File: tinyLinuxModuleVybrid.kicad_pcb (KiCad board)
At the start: 4 copper layers, 85 x 56 mm, 164 parts, among them IC1 LAN8720, IC2 USB2514B, IC3 MAX3221, IC4 TPS2033, IC5 WE-TVS-82400274, IC6 WE-TVS-82400274, IC7 TLV62065, M1 SCREW, M2 SCREW, M3 SCREW, M4 SCREW, M5 SCREW, M6 SCREW, M7 SCREW, M8 SCREW, Q1 2N7002BKT, Q2 2N7002BKT, Q3 2N7002BKT, U1 LT3958, X1 CONN_02x50, X10 MagJack100, X11 MICROSD, X12 CONN_01x03, X2 CONN_02x50, X3 USB4DUAL, X4 CONN_02x25, X5 ARM_JTAG_10, X6 USB4DUAL, X7 CONN_02x20, X8 CONN_02x14, X9 USB5, Y1 24M,18p

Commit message: LILY Antenne hinzugefügt
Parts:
- added REF**: NANO_SIM_693043020611, Connector:NANO_SIM_693043020611, F.Cu at (22.0, -51.4)
- moved REF** 108.0 mm to (25.3, -26.1), turned to 90 degrees
- moved X? 96.1 mm to (39.1, -8.16)
- moved U1 46.9 mm to (75.1, -27.8)
- moved L1 45.1 mm to (70.8, -30.2)
- moved REF** 22.3 mm to (7.78, -26.8)
- moved REF** 20.2 mm to (4.51, -15.4), turned to 90 degrees
- moved REF** 13.2 mm to (5.04, -39.9)
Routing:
- net GND: track 164.5 -> 406.0 mm, vias 99 -> 111
- net (no net): track 1257.1 -> 1033.4 mm, vias 56 -> 33
- net +3V3: track 120.9 -> 273.9 mm, vias 30 -> 39
- net /PTC6: track 0.00 -> 55.8 mm, vias 0 -> 3
- net +5V: track 117.3 -> 69.6 mm, vias 7 -> 1
- net /PTE21: track 33.8 -> 1.46 mm, vias 3 -> 0
- net /PTC4: track 76.4 -> 45.7 mm, vias 3 -> 1
- net /PTE15: track 30.6 -> 2.03 mm, vias 3 -> 0
- net /PTE17: track 26.6 -> 1.46 mm, vias 3 -> 1
- net /PTC1: track 73.1 -> 56.7 mm, vias 3 -> 4
- net /PTE9: track 35.4 -> 20.4 mm, vias 3 -> 1
- net /PTE19: track 22.5 -> 7.50 mm, vias 3 -> 2
- net /PTE13: track 3.10 -> 17.6 mm, vias 0 -> 1
- net /PTE10: track 0.00 -> 13.5 mm, vias 0 -> 1
- net /Communication/RMII_TXEN: track 15.6 -> 2.56 mm, vias 2 -> 0
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
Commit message: added some footprints
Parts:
- removed C1, C12, C14, C15, C33 (x3), C35, C37, C38, C39, C40 (x3): 22u,10V, Passives:C1206N
- removed C10, C11, C2, C3, C32 (x3), C4, C8: 100n, Passives:C0402N
- removed C16, C17, C18, C19, C20, C21, C22, C41: 1u,10V,X5R, Passives:C0402N
- removed C23, C24, C25, C26: 10p, Passives:C0402N
- removed C27, C28, C29, C30, C31: 100n,16V, Passives:C0402N
- removed C34: 220u,16V, Passives:CPOL_THT_D6.3_G2.5
- removed C36: 22p,25V, Passives:C0402N
- removed C6, C7: 18p, Passives:C0402N
- removed FID1, FID2, FID3 (x3), FID4: FIDUCIAL, Mechanical:FIDUCIAL_1mm
- removed IC1: LAN8720, Communication:LAN8720_QFN33
- removed IC2: USB2514B, USB_IC:USB251xB_QFN36
- removed IC3: MAX3221, Communication:MAX3221_TSSOP
- removed IC4: TPS2033, USB_IC:TPS203xD
- removed IC5, IC6: WE-TVS-82400274, USB_IC:WE-TVS-82400274_SC70
- removed IC7: TLV62065, Switcher_IC:TLV62065_WSON
- removed L1: 600R@100M, Passives:B0402N
- removed L1: DRQ125, myfootprint:DRQ125
- removed L2: 1uH,2A, Passives:L1008N
- removed LED1 (x3): G, Passives:LED0603N
- removed LED2 (x3): Y, Passives:LED0603N
- removed LED3 (x3): B, Passives:LED0603N
- removed M1, M2, M3, M4: SCREW, Mechanical:SCREW_M1.5
- removed M5, M6, M7, M8: SCREW, Mechanical:SCREW_M2.5
- removed PTC1: 2A, Passives:PTC1210N
- removed Q1 (x3), Q2 (x3), Q3 (x3): 2N7002BKT, Transistor:SOT416_GSD
- removed R10 (x3), R11 (x3), R13, R16, R35 (x3), R36 (x3), R6, R7, R8 (x3), R9 (x3): 10k, Passives:R0402N
- removed R12, R14: 470, Passives:R0402N
- removed R15, R25 (x3), R26 (x3), R27 (x3), R31 (x3), R32 (x3), R33 (x3): 1k, Passives:R0402N
- removed R17, R5: 12k, Passives:R0402N
- removed R18, R19, R20, R21: 49.9R, Passives:R0402N
- removed R22: 22R, Passives:R0402N
- removed R29: 390k, Passives:R0402N
- removed R30: 86.6k, Passives:R0402N
- removed R37: 22, Passives:R0402N
- removed REF**: MPU-9250, Sensors:MPU-9250
- removed REF**: LILY-W1, Communication:UBLOX-LILY-W1
- removed REF**: NEO-M8P, Communication:UBLOX_NEO-M8P
- removed REF**: Toby L210, Communication:UBLOX_TOBY_L210
- removed REF**: NANO_SIM_693043020611, Connector:NANO_SIM_693043020611
- removed U1: LT3958, myfootprint:UHE28MA
- removed V1: 5V, Passives:V0805N
- removed X1, X2: CONN_02x50, Connector:Hirose-DF40-100DP
- removed X10: MagJack100, Connector:MagJack100_Standard
- removed X11 (x3): MICROSD, Memory:MICROSD_STD
- removed X12: CONN_01x03, Connector:PinHD-90-2.54-01x03-THT
- removed X3, X6: USB4DUAL, Connector:USB4DUAL_A
- removed X4 (x3): CONN_02x25, Connector:Hirose-DF40-50DP
- removed X5: ARM_JTAG_10, Connector:PinBox-1.27-02x05-SMT
- removed X7: CONN_02x20, Connector:PinHD-2.54-02x20-THT
- removed X8: CONN_02x14, Connector:PinHD-2.54-02x14-THT
- removed X9: USB5, Connector:USB5_MicroUSB_Fixed
- removed X?: CONN_04x50, myfootprint:VybridBoard
- removed Y1: 24M,18p, Crystals:Crystal_3.2x2.5
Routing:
- net (no net): track 1033.4 -> 8.63 mm, vias 33 -> 0
- net GND: track 406.0 -> 0.00 mm, vias 111 -> 0
- net +3V3: track 273.9 -> 0.00 mm, vias 39 -> 0
- net /PTC3: track 118.1 -> 0.00 mm, vias 4 -> 0
- net /PTC0: track 95.8 -> 0.00 mm, vias 2 -> 0
- net +5V: track 69.6 -> 0.00 mm, vias 1 -> 0
- net /PTC5: track 60.8 -> 0.00 mm, vias 4 -> 0
- net /PTC2: track 58.7 -> 0.00 mm, vias 2 -> 0
- net Net-(V1-Pad1): track 58.4 -> 0.00 mm
- net /PTC1: track 56.7 -> 0.00 mm, vias 4 -> 0
- net /PTC6: track 55.8 -> 0.00 mm, vias 3 -> 0
- net Net-(C34-Pad+): track 54.7 -> 0.00 mm, vias 3 -> 0
- net /PTC4: track 45.7 -> 0.00 mm, vias 1 -> 0
- net /PTD21: track 32.1 -> 0.00 mm, vias 4 -> 0
- net /PTE7: track 31.2 -> 0.00 mm, vias 4 -> 0
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- removed copper zone on F.Cu, net +3V3
- removed copper zone on F.Cu, net +5V
- removed copper zone on B.Cu, net /Communication/USB_VBUS_OUT
- removed copper zone on F.Cu, net GND
- removed copper zone on F.Cu, net Net-(IC7-Pad2)
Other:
- board outline removed

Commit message: adjusted power supply
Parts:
- added C101: 100n, Passives:C0402N, F.Cu at (9.58, 1.64)
- added C102: 22u,10V, Passives:C1206N, F.Cu at (4.35, 9.26)
- added C103: 1u,10V,X5R, Passives:C0402N, F.Cu at (9.05, 5.45)
- added C104: 1u,10V,X5R, Passives:C0402N, F.Cu at (8.54, -5.72)
- added C201: 1u,10V,X5R, Passives:C0402N, F.Cu at (8.31, -2.93)
- added C202, C203, C204, C205, C206: 1u,10V,X5R, Passives:C0402N, F.Cu at (0.00, 0.00)
- added C207, C208, C209, C210, C401, C402, C403, C405, C410: 10p, Passives:C0402N, F.Cu at (0.00, 0.00)
- added C211, C501, C512, C513, C514, C515: 22u,10V, Passives:C1206N, F.Cu at (0.00, 0.00)
- added C301: 68p, 50V, Passives:C0402N, F.Cu at (0.00, 0.00)
- added C302: 15p, 50V, Passives:C0402N, F.Cu at (0.00, 0.00)
- added C303: 8.2p, 50V, Passives:C0402N, F.Cu at (0.00, 0.00)
- added C304: 10n, 50V, Passives:C0402N, F.Cu at (0.00, 0.00)
- added C305, C315: 100n, 16V, Passives:C0402N, F.Cu at (0.00, 0.00)
- added C308, C309, C311, C313: 47p, 50V, Passives:C0402N, F.Cu at (0.00, 0.00)
- added C310, C314: 33p, 50V, Passives:C0402N, F.Cu at (0.00, 0.00)
- added C312: 27p, 50V, Passives:C0402N, F.Cu at (0.00, 0.00)
- added C404, C502, C503, C504, C505, C506, C509, C510, C511, C601, C602, C801, C802, C803, C804, C805: 100n, Passives:C0402N, F.Cu at (0.00, 0.00)
- added C406: 2.2u, Passives:C1206N, F.Cu at (0.00, 0.00)
- added C409, C411: C, Passives:C0402N, F.Cu at (0.00, 0.00)
- added C507, C508: 18p, Passives:R0402N, F.Cu at (0.00, 0.00)
- added C603, C702, C705: 10n, 16V, Passives:C0402N, F.Cu at (0.00, 0.00)
- added C703: 680p, 16V, Passives:C0402N, F.Cu at (0.00, 0.00)
- added C704: 22p, 25V, Passives:C0402N, F.Cu at (0.00, 0.00)
- added C706: 0.47 uF, X7R, 10V, Passives:C0402N, F.Cu at (0.00, 0.00)
- added C707: 4.7 uF, X5R, 10V, Passives:C0402N, F.Cu at (0.00, 0.00)
- added C708: 10 nF, X7R, 10V, Passives:C0402N, F.Cu at (0.00, 0.00)
- added C709: 2.2 uF, X7R,100V, Passives:C1210N, F.Cu at (12.7, 0.12)
- added C710: 470n, 25V, Passives:C0603N, F.Cu at (0.00, 0.00)
- added C711: 22 uF, X5R, 16V, Passives:C1210N, F.Cu at (0.00, 0.00)
- added C712: 22u, 25V, Passives:C1210N, F.Cu at (0.00, 0.00)
- added C714, C719: 22u, 10V, Passives:V1206N, F.Cu at (0.00, 0.00)
- added C715: 10u,25V, Passives:V1210N, F.Cu at (0.00, 0.00)
- added C716: 3.3n,25V, Passives:C0402N, F.Cu at (0.00, 0.00)
- added C717: 22p, 10V, Passives:C0402N, F.Cu at (0.00, 0.00)
- added C718: 47u,6.3V, Passives:C1210N, F.Cu at (0.00, 0.00)
- added D301, D302, D303, D304, D305, D306: DP, Passives:D_0402, F.Cu at (0.00, 0.00)
- added D701: 10MQ100N, Passives:D_SOD124, F.Cu at (0.00, 0.00)
- added D702: MBRA340T3G, Passives:D_214_AC, F.Cu at (0.00, 0.00)
- added FID101, FID102, FID103, FID104: FIDUCIAL, Mechanical:FIDUCIAL_1mm, F.Cu at (0.00, 0.00)
- added IC201: LAN8720, Communication:LAN8720_QFN33, F.Cu at (0.00, 0.00)
- added IC501: USB2514B, USB_IC:USB251xB_QFN36, F.Cu at (15.7, -8.01)
- added IC502: WE-TVS-82400274, USB_IC:WE-TVS-82400274_SC70, F.Cu at (7.11, 1.50)
- added IC503: TPS2033, USB_IC:TPS203xD, F.Cu at (0.00, 0.00)
- added IC504: WE-TVS-82400274, USB_IC:WE-TVS-82400274_SC70, F.Cu at (0.00, 0.00)
- added IC702: TPS62143RGTR, Switcher_IC:TPS62143, F.Cu at (0.00, 0.00)
- added IC703: TLV62065, Switcher_IC:TLV62065_WSON, F.Cu at (0.00, 0.00)
- added IC801: BME680, Sensors:BME680, F.Cu at (0.00, 0.00)
- added L201: 600R@100M, Passives:B0402N, F.Cu at (0.00, 0.00)
- added L301, L302: 68n, Passives:L0402N, F.Cu at (0.00, 0.00)
- added L601: 27n, Passives:L0402N, F.Cu at (0.00, 0.00)
- added L701: DRQ125, myfootprint:DRQ125, F.Cu at (-29.5, -55.9)
- added L703: 1uH,2A, Passives:L1008N, F.Cu at (0.00, 0.00)
- added LED101: G, Passives:LED0603N, F.Cu at (0.00, 0.00)
- added LED102: Y, Passives:LED0603N, F.Cu at (0.00, 0.00)
- added LED103: B, Passives:LED0603N, F.Cu at (0.00, 0.00)
- added LED301: GREEN, Passives:LED0603N, F.Cu at (0.00, 0.00)
- added M101, M103, M105, M107: SCREW, Mechanical:SCREW_M1.5, F.Cu at (0.00, 0.00)
- added M102, M104, M106, M108: SCREW, Mechanical:SCREW_M2.5, F.Cu at (0.00, 0.00)
- added Q101, Q102, Q103, Q301: 2N7002BKT, Transistor:SOT416_GSD, F.Cu at (0.00, 0.00)
- added R101, R102, R103, R104, R105, R106, R107, R201, R203, R206, R506, R603, R707, R708, R709, R803, R804: 10k, Passives:R0402N, F.Cu at (0.00, 0.00)
- added R108, R109: 22, Passives:R0402N, F.Cu at (0.00, 0.00)
- added R110, R111, R112, R113, R114, R115, R205, R301, R302: 1k, Passives:R0402N, F.Cu at (0.00, 0.00)
- added R202, R204: 470, Passives:R0402N, F.Cu at (0.00, 0.00)
- added R207, R505: 12k, Passives:R0402N, F.Cu at (0.00, 0.00)
- added R208, R209, R210, R211: 49.9R, Passives:R0402N, F.Cu at (0.00, 0.00)
- added R305, R306, R307, R402, R403, R602, R604: 0, Passives:R0402N, F.Cu at (0.00, 0.00)
- added R401: 33k, Passives:R0402N, F.Cu at (0.00, 0.00)
- added R501, R502, R503, R504, R711, R714: 100k, Passives:R0402N, F.Cu at (0.00, 0.00)
- added R601: 10 Ω ± 10%, min 0.250 W, Passives:R0402N, F.Cu at (0.00, 0.00)
- added R701: 470k, Passives:V0402N, F.Cu at (0.00, 0.00)
- added R702: 15k, Passives:R0402N, F.Cu at (0.00, 0.00)
- added R703: 392k, Passives:R0402N, F.Cu at (0.00, 0.00)
- added R704: 66.5k, Passives:R0402N, F.Cu at (0.00, 0.00)
- added R705: 22k, Passives:R0402N, F.Cu at (0.00, 0.00)
- added R706: 41.2k, Passives:R0402N, F.Cu at (0.00, 0.00)
- added R710, R712: 390k, Passives:R0402N, F.Cu at (0.00, 0.00)
- added R713: 86.6k, Passives:R0402N, F.Cu at (0.00, 0.00)
- added R801, R802: 4,7k, Passives:R0402N, F.Cu at (0.00, 0.00)
- added U301: U-BLOX-TOBY-L2, Communication:UBLOX_TOBY_L210, F.Cu at (145.0, 25.2)
- added U401: U-BLOX_LILY-W1, Communication:UBLOX-LILY-W1, F.Cu at (155.9, 45.3)
- added U601: U-BLOX-NEO-M8N, Communication:UBLOX_NEO-M8P, F.Cu at (137.8, 48.6)
- added U701: LT3958, myfootprint:UHE28MA, F.Cu at (0.00, 0.00)
- added U801: MPU-9250, Sensors:MPU-9250, F.Cu at (0.00, 0.00)
- added X101: MICROSD, Memory:MICROSD_STD, B.Cu at (108.1, 22.2)
- added X104: VybridBoard, myfootprint:VybridBoard, F.Cu at (105.3, 28.1)
- added X105: ARM_JTAG_10, Connector:PinBox-1.27-02x05-SMT, F.Cu at (-22.9, 2.66)
- added X301, X303, X601: ANT, Connector:U.FL-R-SMT, F.Cu at (0.00, 0.00)
- added X302: SIMcard, Connector:NANO_SIM_693043020611, B.Cu at (144.2, 19.4)
- added X401: ANT, Connector:U.FL-R-SMT, F.Cu at (170.9, 1.64)
- added Y501: 24M,18p, Crystals:Crystal_3.2x2.5, F.Cu at (0.00, 0.00)

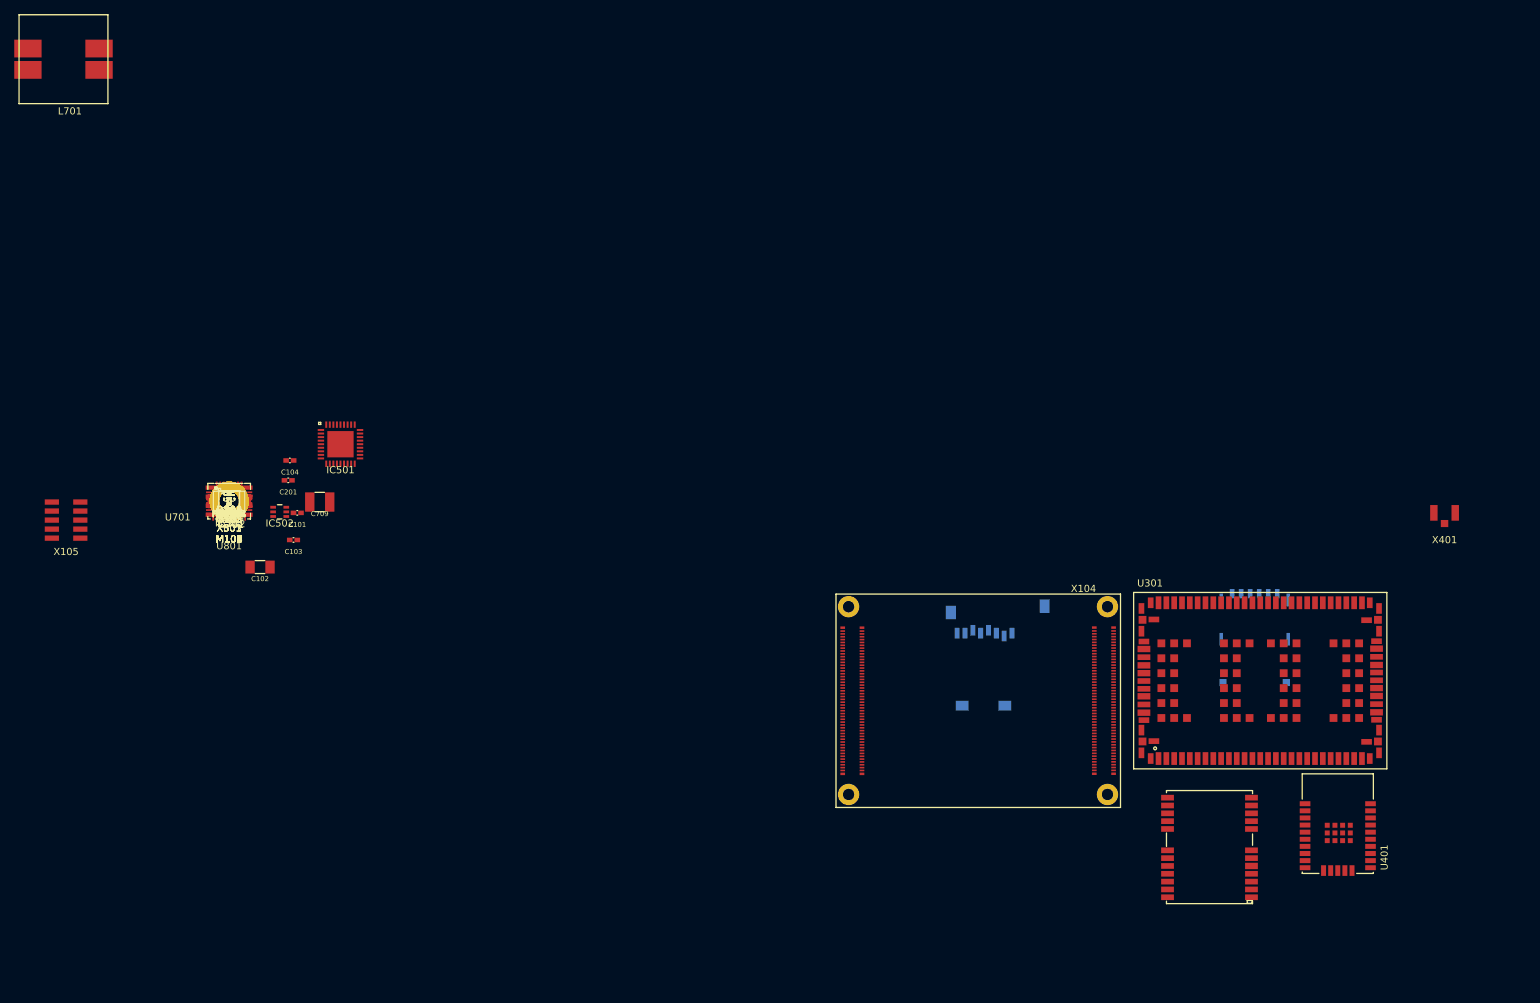
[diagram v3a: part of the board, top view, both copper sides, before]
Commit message: adjusted power supply and sensors
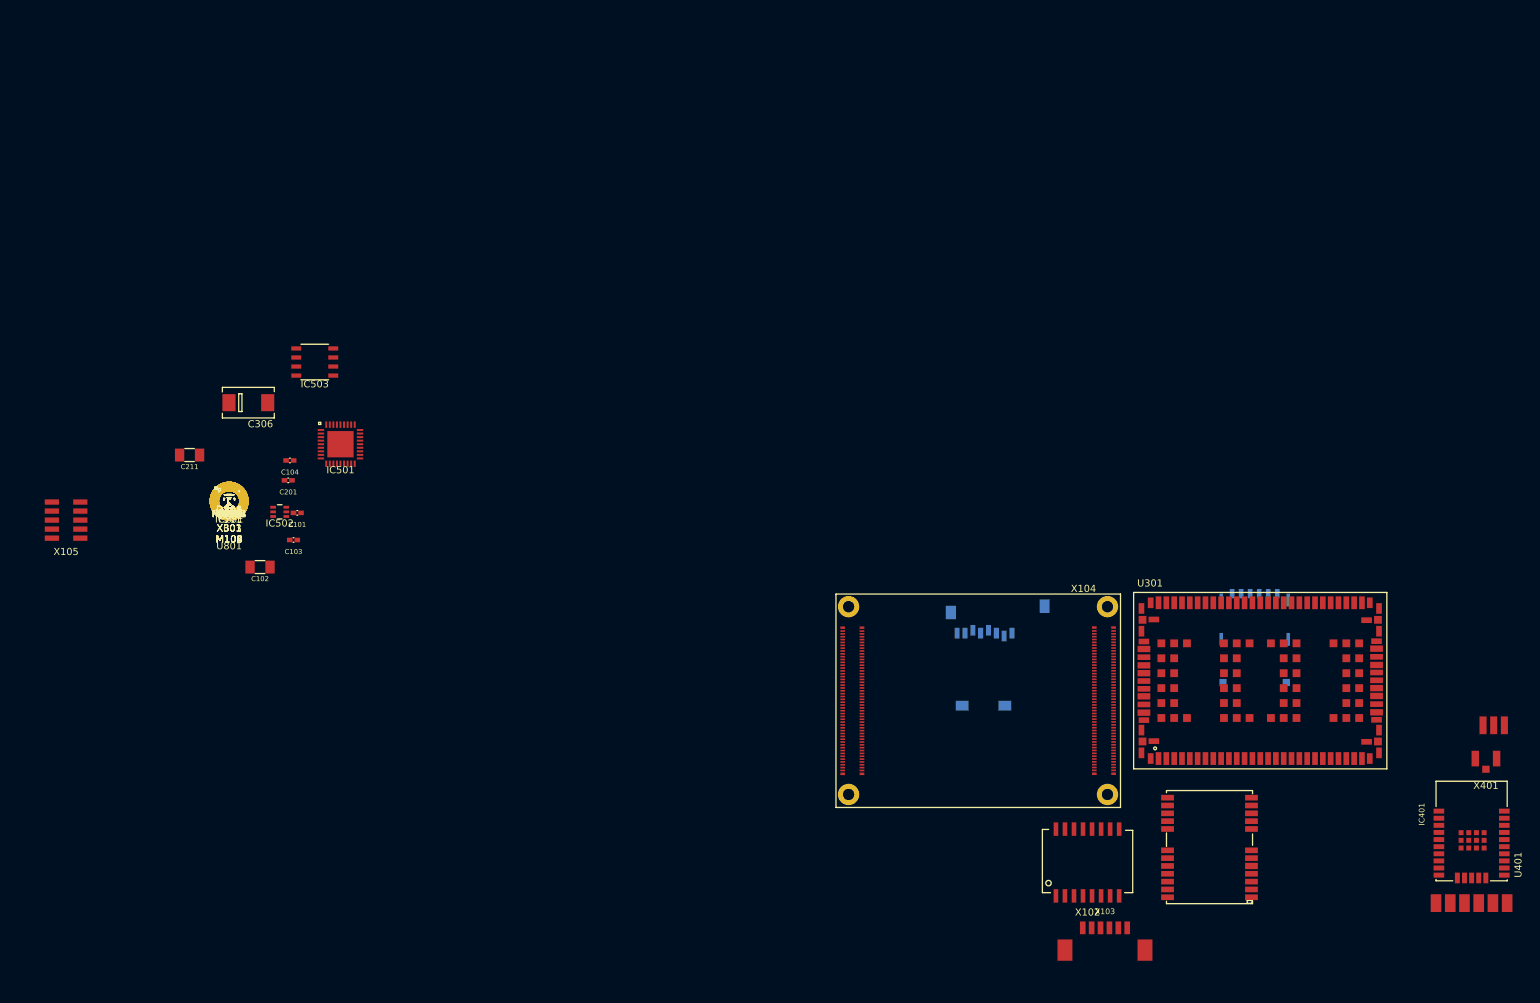
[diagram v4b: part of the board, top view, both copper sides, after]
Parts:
- removed C702, C705: 10n, 16V, Passives:C0402N
- removed C703: 680p, 16V, Passives:C0402N
- removed C704: 22p, 25V, Passives:C0402N
- removed C706: 0.47 uF, X7R, 10V, Passives:C0402N
- removed C707: 4.7 uF, X5R, 10V, Passives:C0402N
- removed C708: 10 nF, X7R, 10V, Passives:C0402N
- removed C709: 2.2 uF, X7R,100V, Passives:C1210N
- removed C710: 470n, 25V, Passives:C0603N
- removed C711: 22 uF, X5R, 16V, Passives:C1210N
- removed C712: 22u, 25V, Passives:C1210N
- removed C714, C719: 22u, 10V, Passives:V1206N
- removed C715: 10u,25V, Passives:V1210N
- removed C716: 3.3n,25V, Passives:C0402N
- removed C717: 22p, 10V, Passives:C0402N
- removed C718: 47u,6.3V, Passives:C1210N
- removed D701: 10MQ100N, Passives:D_SOD124
- removed D702: MBRA340T3G, Passives:D_214_AC
- removed IC702: TPS62143RGTR, Switcher_IC:TPS62143
- removed IC703: TLV62065, Switcher_IC:TLV62065_WSON
- removed L701: DRQ125, myfootprint:DRQ125
- removed L703: 1uH,2A, Passives:L1008N
- removed M101, M103, M105, M107: SCREW, Mechanical:SCREW_M1.5
- removed R701: 470k, Passives:V0402N
- removed R702: 15k, Passives:R0402N
- removed R703: 392k, Passives:R0402N
- removed R704: 66.5k, Passives:R0402N
- removed R705: 22k, Passives:R0402N
- removed R706: 41.2k, Passives:R0402N
- removed R707, R708, R709, R803, R804: 10k, Passives:R0402N
- removed R710, R712: 390k, Passives:R0402N
- removed R711, R714: 100k, Passives:R0402N
- removed R713: 86.6k, Passives:R0402N
- removed U701: LT3958, myfootprint:UHE28MA
- added C306: 330u, 16V, Passives:T520D, F.Cu at (2.70, -13.8)
- added C806: 100n, Passives:C0402N, F.Cu at (0.00, 0.00)
- added D101: DP, Passives:D_0402, F.Cu at (0.00, 0.00)
- added IC401: WM-294, Communication:WM-294, F.Cu at (174.7, 44.0)
- added R116, R117: Anpassen, Passives:R0402N, F.Cu at (0.00, 0.00)
- added R118, R119, R120, R121: 75, Passives:R0402N, F.Cu at (0.00, 0.00)
- added R303: 0, Passives:R0402N, F.Cu at (0.00, 0.00)
- added R304: R, Passives:R0402N, F.Cu at (0.00, 0.00)
- added R715: 510k, Passives:R0402N, F.Cu at (0.00, 0.00)
- added R716, R718: 162k, Passives:R0402N, F.Cu at (0.00, 0.00)
- added R717: 649k, Passives:R0402N, F.Cu at (0.00, 0.00)
- added R719, R720: 499k, Passives:R0402N, F.Cu at (0.00, 0.00)
- added X102: LAN_Transformer, Communication:UL94-V0, F.Cu at (120.7, 50.6)
- added X103: CONN_01x06, Connector:MLX127_53398_SMD-06, F.Cu at (123.1, 62.5)
- moved X401 35.0 mm to (176.7, 36.2)
- moved IC503 23.0 mm to (12.0, -19.6)
- moved U401 18.8 mm to (174.7, 46.4)
- moved C211 8.54 mm to (-5.56, -6.48)
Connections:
- net Net-(C409-Pad1) renamed /Communication/LILY/RF
- net Net-(R402-Pad2) renamed /Communication/LILY/USB-
- net Net-(R403-Pad2) renamed /Communication/LILY/USB+
- net Net-(U801-Pad22) renamed /Sensors/~CS
- C804 pad 1: +3V3 -> Net-(C804-Pad1)
- U801 pad 13: +3V3 -> Net-(C804-Pad1)
- U801 pad 9: GND -> Net-(U801-Pad9)
- X104 pad M1: (no net) -> Net-(X104-PadM1)
- X104 pad M2: (no net) -> Net-(X104-PadM2)
- X104 pad M3: (no net) -> Net-(X104-PadM3)
- X104 pad M4: (no net) -> Net-(X104-PadM4)
- X104 pad M5: (no net) -> Net-(X104-PadM5)
- X104 pad M6: (no net) -> Net-(X104-PadM6)
- X104 pad M7: (no net) -> Net-(X104-PadM7)
- X104 pad M8: (no net) -> Net-(X104-PadM8)
- X301 pad P: (no net) -> GND
- X303 pad P: (no net) -> GND
- X401 pad P: (no net) -> GND
- X601 pad P: (no net) -> GND
